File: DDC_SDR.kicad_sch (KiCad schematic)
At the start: 104 parts, among them J1 Filter, J2 S11, J3 Filter, J4 S21_OUT, J5 AWG_OUT, J6 PMOD, Q1 2N7002, Q2 2N7002, U1 74LVC1G3157GW, U2 TPH2501-TR, U3 TPH2501-TR, U4 MS9280, U5 MS9708, U6 74LVC1G3157GW, U7 ICE40UP5K-SG48ITR

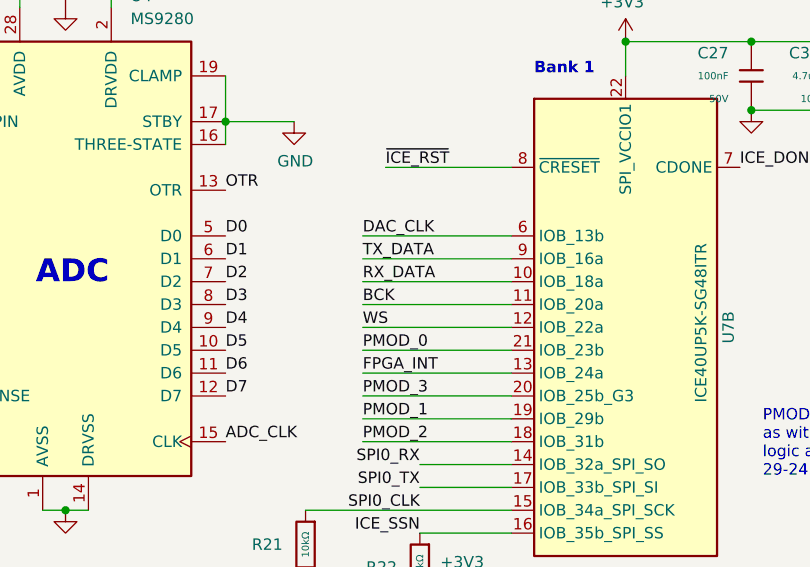
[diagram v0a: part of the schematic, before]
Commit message: Lots of signal traces wided
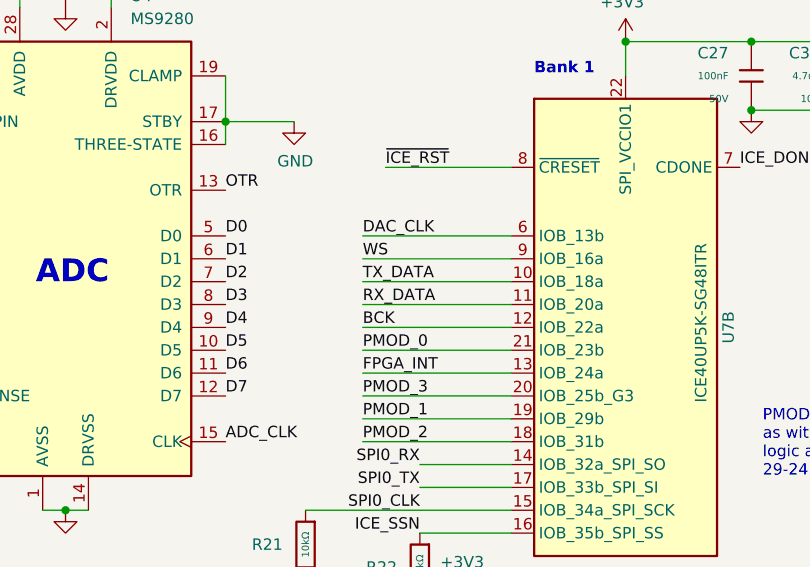
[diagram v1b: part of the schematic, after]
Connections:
- net BCK: now also U7.12 (IOB_22a); no longer U7.11 (IOB_20a)
- net RX_DATA: now also U7.11 (IOB_20a); no longer U7.10 (IOB_18a)
- net TX_DATA: now also U7.10 (IOB_18a); no longer U7.9 (IOB_16a)
- net WS: now also U7.9 (IOB_16a); no longer U7.12 (IOB_22a)
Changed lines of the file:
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@@
 	)
 	(label "RX_DATA"
-		(at 160.02 60.96 0)
+		(at 160.02 63.5 0)
 		(effects
 			(font
@@
 	)
 	(label "WS"
-		(at 160.02 66.04 0)
+		(at 160.02 58.42 0)
 		(effects
 			(font
@@
 	)
 	(label "TX_DATA"
-		(at 160.02 58.42 0)
+		(at 160.02 60.96 0)
 		(effects
 			(font
@@
 	)
 	(label "BCK"
-		(at 160.02 63.5 0)
-		(effects
-			(font
+		(at 160.02 66.04 0)
+		(effects
+			(font

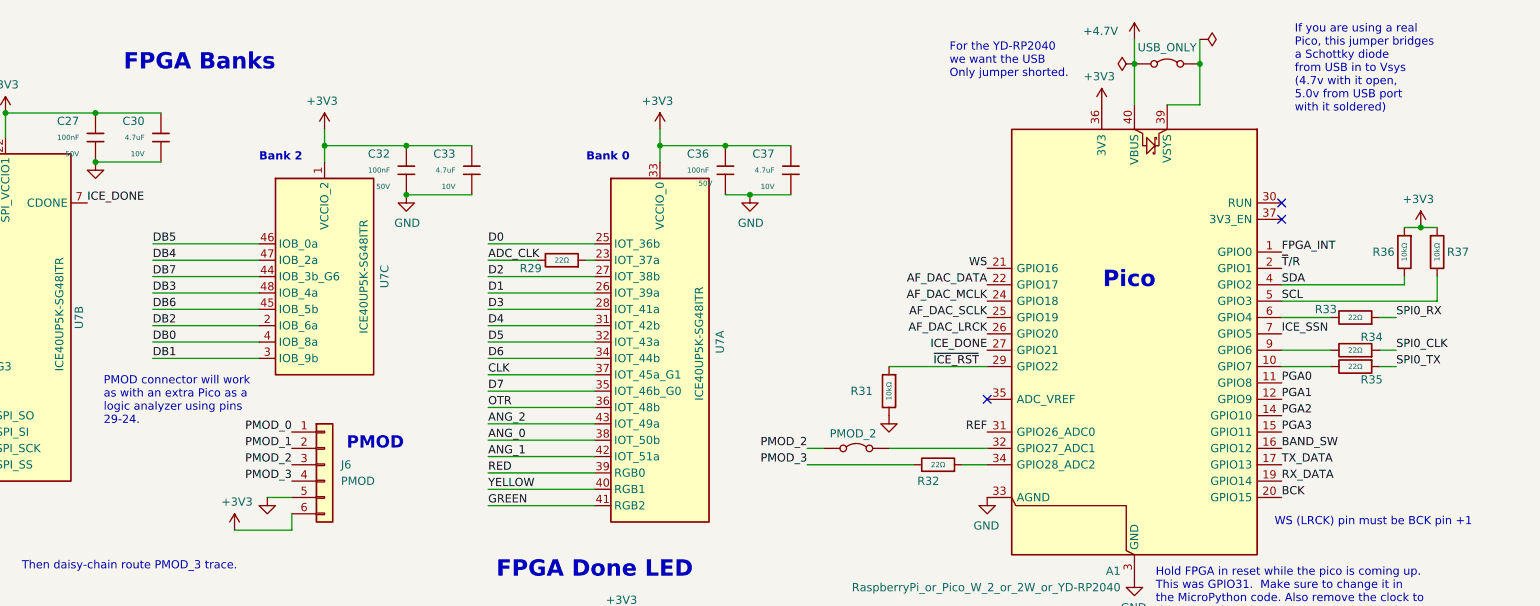
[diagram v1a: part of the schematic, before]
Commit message: PAM and LEDs
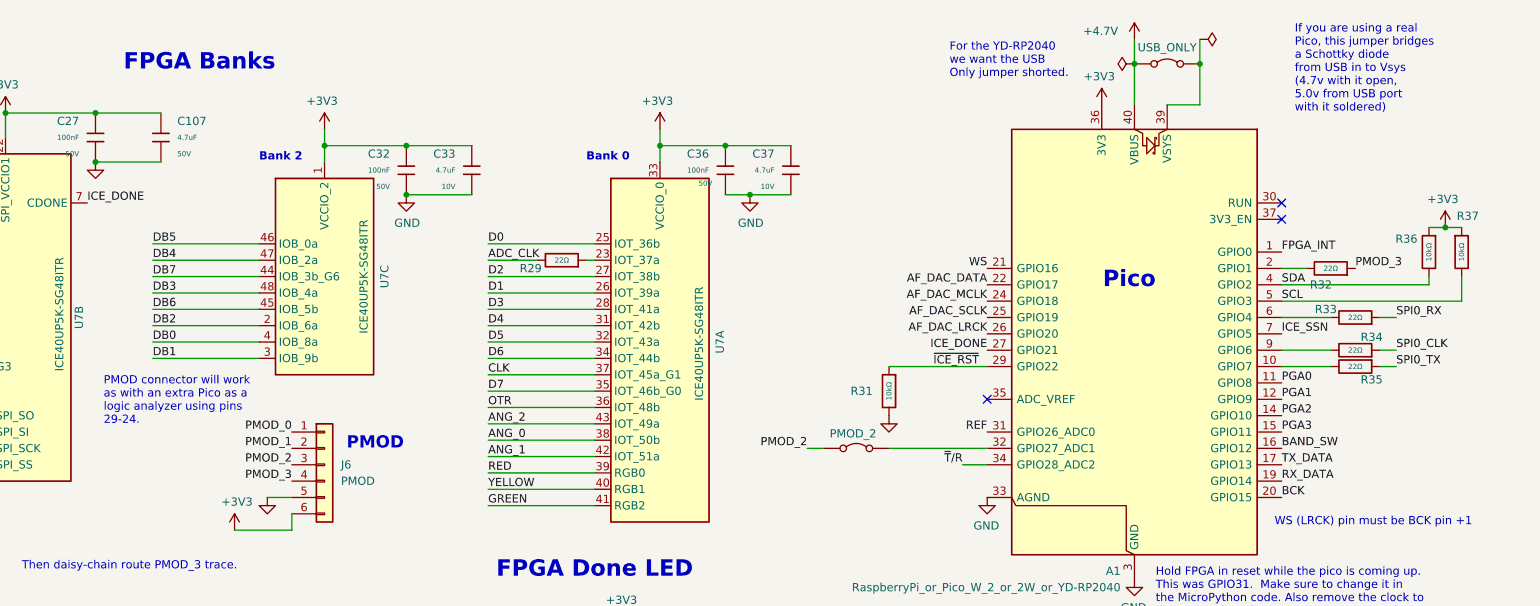
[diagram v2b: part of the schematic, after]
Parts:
- removed C30: 4.7uF, PCM_JLCPCB:C_0402, symbol PCM_JLCPCB-Capacitors:0402,4.7uF
- added C107: 4.7uF, PCM_JLCPCB:C_1206, symbol PCM_JLCPCB-Capacitors:1206,4.7uF
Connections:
- net +3V3: now also C107.1
- net GND: now also C107.2
- net PMOD_3: now also R32.1; no longer R32.2
- net ~{T}/R: now also A1.34 (GPIO28_ADC2); no longer A1.2 (GPIO1)
- new net: A1.2 (GPIO1), R32.2
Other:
- moved on the sheet: R32, R36, R37

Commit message: Added test points
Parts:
- added JP8: +3V3, Jumper:SolderJumper-2_P1.3mm_Bridged2Bar_RoundedPad1.0x1.5mm, symbol Jumper:Jumper_2_Bridged
- added TP14, TP15: U15, TestPoint:TestPoint_THTPad_D2.5mm_Drill1.2mm, symbol Connector:TestPoint
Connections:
- net +3V3: now also JP8.2 (B); no longer A1.36 (3V3)
- net A+: now also TP15.1
- net O+: now also TP14.1
- new net: A1.36 (3V3), JP8.1 (A)

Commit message: Added Prototype Area
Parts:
- TP1, TP14, TP15, TP2, TP3: footprint TestPoint:TestPoint_THTPad_D2.5mm_Drill1.2mm -> RP2040_minimal:TestPoint_THTPad_D2.5mm_Drill1.2mm
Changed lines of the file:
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@@
 			)
 		)
-		(property "Footprint" "TestPoint:TestPoint_THTPad_D2.5mm_Drill1.2mm"
+		(property "Footprint" "RP2040_minimal:TestPoint_THTPad_D2.5mm_Drill1.2mm"
 			(at 97.79 38.1 0)
 			(hide yes)
@@
 			)
 		)
-		(property "Footprint" "TestPoint:TestPoint_THTPad_D2.5mm_Drill1.2mm"
+		(property "Footprint" "RP2040_minimal:TestPoint_THTPad_D2.5mm_Drill1.2mm"
 			(at 92.71 237.49 0)
 			(hide yes)
@@
 			)
 		)
-		(property "Footprint" "TestPoint:TestPoint_THTPad_D2.5mm_Drill1.2mm"
+		(property "Footprint" "RP2040_minimal:TestPoint_THTPad_D2.5mm_Drill1.2mm"
 			(at 64.77 234.95 0)
 			(hide yes)
@@
 			)
 		)
-		(property "Footprint" "TestPoint:TestPoint_THTPad_D2.5mm_Drill1.2mm"
+		(property "Footprint" "RP2040_minimal:TestPoint_THTPad_D2.5mm_Drill1.2mm"
 			(at 193.04 242.57 0)
 			(hide yes)
@@
 			)
 		)
-		(property "Footprint" "TestPoint:TestPoint_THTPad_D2.5mm_Drill1.2mm"
+		(property "Footprint" "RP2040_minimal:TestPoint_THTPad_D2.5mm_Drill1.2mm"
 			(at 83.82 198.12 0)
 			(hide yes)

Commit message: Some 3D models
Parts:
- J2, J4, J5: now fitted
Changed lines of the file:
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@@
 		(on_board yes)
 		(in_pos_files yes)
-		(dnp yes)
+		(dnp no)
 		(property "Reference" "J5"
 			(at 102.5526 231.14 0)
@@
 		(on_board yes)
 		(in_pos_files yes)
-		(dnp yes)
+		(dnp no)
 		(property "Reference" "J2"
 			(at 47.9426 105.41 0)
@@
 		(on_board yes)
 		(in_pos_files yes)
-		(dnp yes)
+		(dnp no)
 		(property "Reference" "J4"
 			(at 102.5526 213.36 0)

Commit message: 3.3VA
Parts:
- added H1: Prototyping Area, RP2040_minimal:Prototype_array, symbol Mechanical:MountingHole
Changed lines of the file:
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@@
+	)
+	(symbol
+		(lib_id "Mechanical:MountingHole")
+		(at 195.58 190.5 0)
+		(unit 1)
+		(body_style 1)
+		(exclude_from_sim no)
+		(in_bom no)
+		(on_board yes)
+		(in_pos_files yes)
+		(dnp no)
+		(fields_autoplaced yes)
+		(property "Reference" "H1"
+			(at 198.12 189.2299 0)
+			(show_name no)
+			(do_not_autoplace no)
+			(effects
+				(font
+					(size 1.27 1.27)
+				)
+				(justify left)
+			)
+		)
+		(property "Value" "Prototyping Area"
+			(at 198.12 191.7699 0)
+			(show_name no)
+			(do_not_autoplace no)
+			(effects
+				(font
+					(size 1.27 1.27)
+				)
+				(justify left)
+			)
+		)
+		(property "Footprint" "RP2040_minimal:Prototype_array"
+			(at 195.58 190.5 0)
+			(hide yes)
+			(show_name no)
+			(do_not_autoplace no)
+			(effects
+				(font
+					(size 1.27 1.27)
+				)
+			)
+		)
+		(property "Datasheet" ""
+			(at 195.58 190.5 0)
+			(hide yes)
+			(show_name no)
+			(do_not_autoplace no)
+			(effects
+				(font
+					(size 1.27 1.27)
+				)
+			)
+		)
+		(property "Description" "Mounting Hole without connection"
+			(at 195.58 190.5 0)
+			(hide yes)
+			(show_name no)
+			(do_not_autoplace no)
+			(effects
+				(font
+					(size 1.27 1.27)
+				)
+			)
+		)
+		(instances
+			(project "DDC_SDR"
+				(path "/7dfef218-ca21-47b0-a8d3-67c7d55cb9d2"
+					(reference "H1")
+					(unit 1)
+				)
+			)
+		)
 	)
 	(symbol

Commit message: 0 disconnects
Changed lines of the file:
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@@
 		(in_pos_files yes)
 		(dnp no)
-		(fields_autoplaced yes)
 		(property "Reference" "A1"
 			(at 362.3467 105.41 0)
@@
 		(lib_id "PCM_JLCPCB-Capacitors:0402,100nF,(2)")
 		(at 127 26.67 0)
-		(mirror y)
 		(unit 1)
 		(body_style 1)
@@
 		(dnp no)
 		(property "Reference" "C22"
-			(at 132.334 24.892 0)
+			(at 121.666 24.892 0)
 			(show_name no)
 			(do_not_autoplace no)
@@
 		)
 		(property "Value" "100nF"
-			(at 126.492 24.892 0)
+			(at 127.508 24.892 0)
 			(show_name no)
 			(do_not_autoplace no)
@@
 		)
 		(property "Footprint" "PCM_JLCPCB:C_0402"
-			(at 128.778 26.67 90)
+			(at 125.222 26.67 90)
 			(hide yes)
 			(show_name no)
@@
 		)
 		(property "Voltage Rated" "50V"
-			(at 124.968 28.7162 0)
+			(at 129.032 28.7162 0)
 			(show_name no)
 			(do_not_autoplace no)

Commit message: 0 errors 0 warnings
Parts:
- J4: value S21_OUT -> S21
- TP1: value U15 -> U2
- TP14: value U15 -> O+
- TP15: value U15 -> A+
- TP2: value U25 -> U3
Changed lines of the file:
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@@
 			)
 		)
-		(property "Value" "U15"
+		(property "Value" "A+"
 			(at 93.98 34.036 0)
 			(show_name no)
@@
 			)
 		)
-		(property "Value" "U25"
+		(property "Value" "U3"
 			(at 88.9 234.442 0)
 			(show_name no)
@@
 			)
 		)
-		(property "Value" "U15"
+		(property "Value" "O+"
 			(at 60.96 230.886 0)
 			(show_name no)
@@
 			)
 		)
-		(property "Value" "S21_OUT"
+		(property "Value" "S21"
 			(at 102.5526 215.9 0)
 			(show_name no)
@@
 			)
 		)
-		(property "Value" "U15"
+		(property "Value" "U2"
 			(at 80.01 194.056 0)
 			(show_name no)
